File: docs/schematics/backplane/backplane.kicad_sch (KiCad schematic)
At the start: 19 parts, among them J1 Transport, J10 Driver, J11 Driver, J12 Driver, J13 INPUT, J14 OUTPUT, J15 BACKGROUND INPUT, J16 BACKGROUND OUTPUT, J17 AGC MICROPHONE, J18 EXT. PROG SWITCH?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

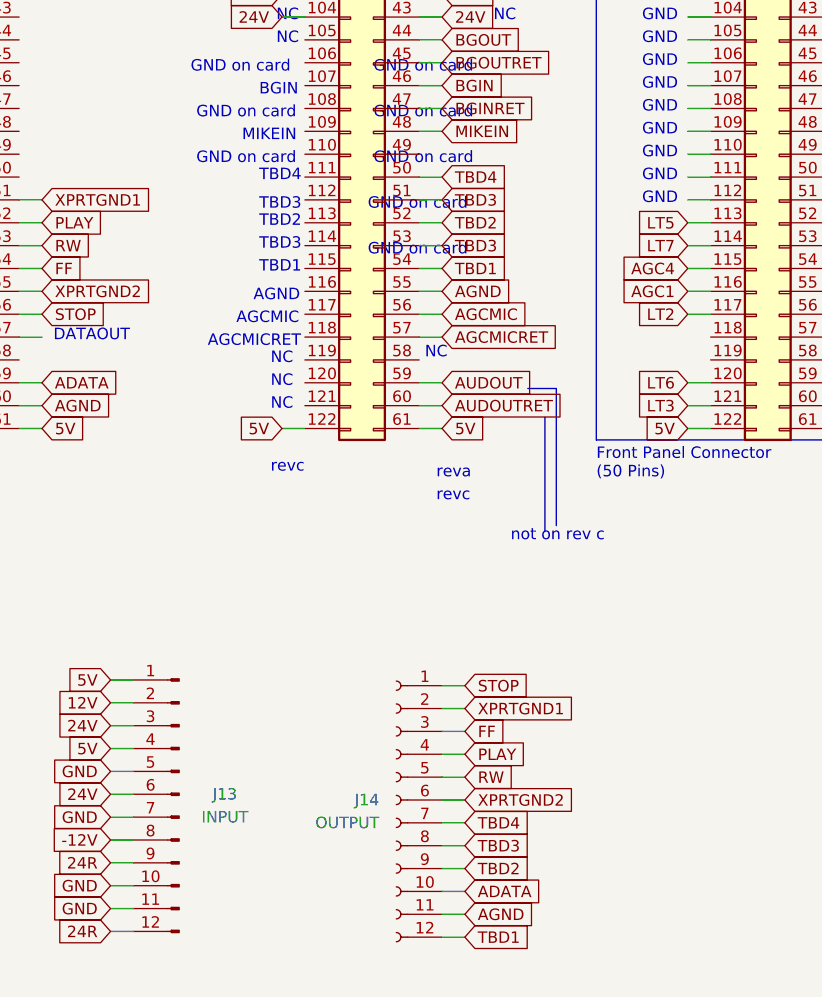
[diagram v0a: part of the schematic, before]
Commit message: finished initial layout and added backplane notes from san jose trip
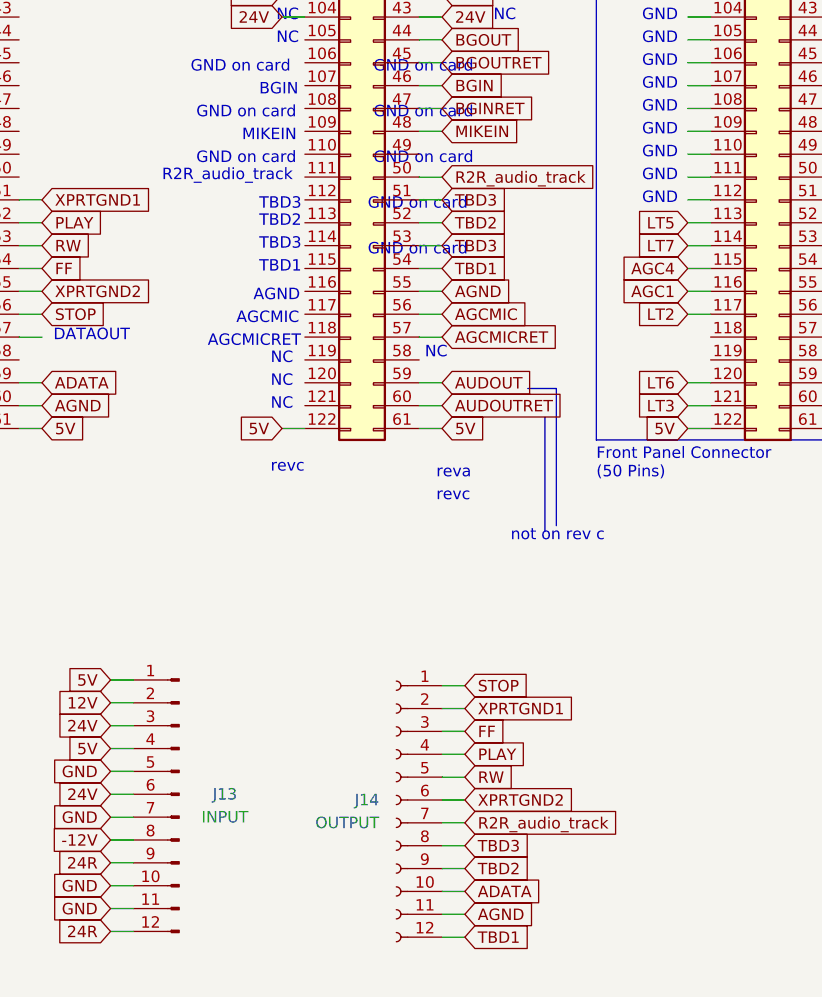
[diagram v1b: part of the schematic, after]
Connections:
- net TBD4 renamed R2R_audio_track
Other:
- note added: "R2R_audio_track"
- note removed: "TBD4"
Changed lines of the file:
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@@
     (effects (font (size 1.27 1.27)) (justify left bottom))
   )
-  (text "TBD4" (at 67.945 153.035 0)
+  (text "R2R_audio_track" (at 57.15 153.035 0)
     (effects (font (size 1.27 1.27)) (justify left bottom))
   )
@@
     )
   )
-  (global_label "TBD4" (shape input) (at 90.805 224.155 0) (fields_autoplaced)
-    (effects (font (size 1.27 1.27)) (justify left))
-    (property "Intersheetrefs" "${INTERSHEET_REFS}" (at 98.4279 224.155 0)
+  (global_label "R2R_audio_track" (shape input) (at 90.805 224.155 0) (fields_autoplaced)
+    (effects (font (size 1.27 1.27)) (justify left))
+    (property "Intersheetrefs" "${INTERSHEET_REFS}" (at 109.3739 224.155 0)
       (effects (font (size 1.27 1.27)) (justify left) hide)
     )
@@
     )
   )
-  (global_label "TBD4" (shape input) (at 88.265 152.4 0) (fields_autoplaced)
-    (effects (font (size 1.27 1.27)) (justify left))
-    (property "Intersheetrefs" "${INTERSHEET_REFS}" (at 95.8879 152.4 0)
-      (effects (font (size 1.27 1.27)) (justify left) hide)
-    )
+  (global_label "R2R_audio_track" (shape input) (at 88.265 152.4 0) (fields_autoplaced)
+    (effects (font (size 1.27 1.27)) (justify left))
+    (property "Intersheetrefs" "${INTERSHEET_REFS}" (at 106.8339 152.4 0)
+      (effects (font (size 1.27 1.27)) (justify left) hide)
+    )

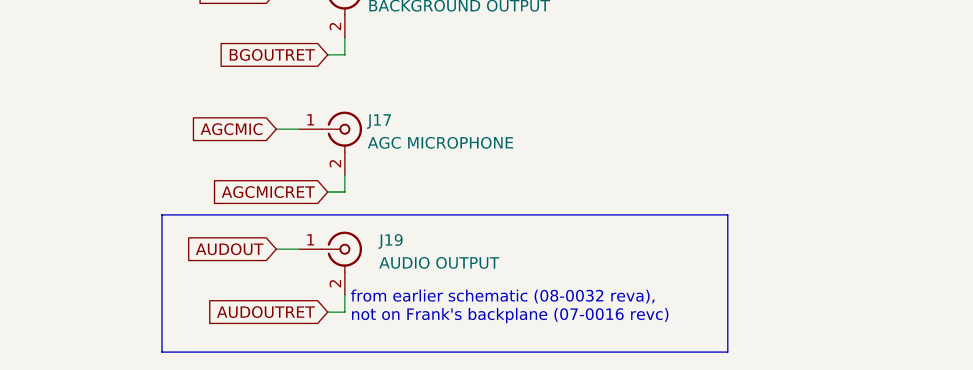
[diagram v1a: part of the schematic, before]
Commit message: tweaked backplane wording to reflect schematic date
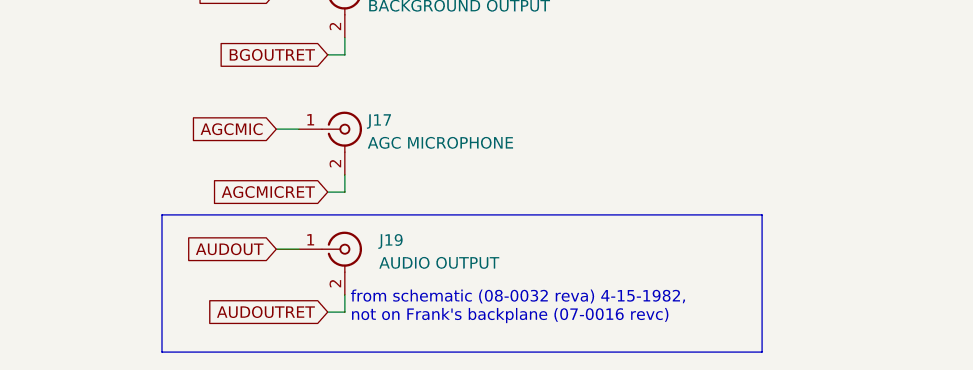
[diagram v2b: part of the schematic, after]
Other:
- note added: "from schematic (08-0032 reva) 4-15-1982, not on Frank's backplane (07-0016 revc)"
- note removed: "from earlier schematic (08-0032 reva), not on Frank's backplane (07-0016 revc)"
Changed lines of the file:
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@@
     (stroke (width 0) (type default))
   )
-  (polyline (pts (xy 128.27 264.795) (xy 191.135 264.795))
+  (polyline (pts (xy 128.27 264.795) (xy 194.945 264.795))
     (stroke (width 0) (type default))
   )
@@
     (stroke (width 0) (type default))
   )
-  (polyline (pts (xy 191.135 264.795) (xy 191.135 249.555))
+  (polyline (pts (xy 194.945 264.795) (xy 194.945 249.555))
     (stroke (width 0) (type default))
   )
@@
     (stroke (width 0) (type default))
   )
-  (polyline (pts (xy 128.27 249.555) (xy 191.135 249.555))
+  (polyline (pts (xy 128.27 249.555) (xy 194.945 249.555))
     (stroke (width 0) (type default))
   )
@@
     (effects (font (size 1.27 1.27)) (justify left bottom))
   )
-  (text "from earlier schematic (08-0032 reva), \nnot on Frank's backplane (07-0016 revc)"
+  (text "from schematic (08-0032 reva) 4-15-1982, \nnot on Frank's backplane (07-0016 revc)"
     (at 149.225 261.62 0)
     (effects (font (size 1.27 1.27)) (justify left bottom))

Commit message: updated some labels on backplane from audio cards
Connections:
- net UNUSED2 renamed R2R_audio_AGC
- net UNUSED3 renamed BGOUT_AGC
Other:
- moved on the sheet: J1, J10, J11, J12, J13, J14, J15, J16, J17, J18, J19, J2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

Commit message: revised all net names to reflect new information about 4 channel audio system
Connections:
- net BCLK renamed aux1_AGC
- net TBD1 renamed aux1_audio_in
- net TBD2 renamed aux2_audio_in
- net TBD3 renamed aux_audio_gnd
- net UNUSED1 renamed aux2_AGC
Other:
- note added: "aux1_audio_in"
- note added: "aux2_audio_in"
- note added: "aux_audio_gnd"
- note removed: "TBD1"
- note removed: "TBD2"
- note removed: "TBD3"
